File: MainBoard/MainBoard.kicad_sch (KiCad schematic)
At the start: 39 parts, among them J1 1761681-3, Q1 BC557, Q10 BC557, Q11 BC557, Q12 BC547, Q13 BC557, Q14 BC557, Q15 BC557, Q2 BC557, Q3 BC557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

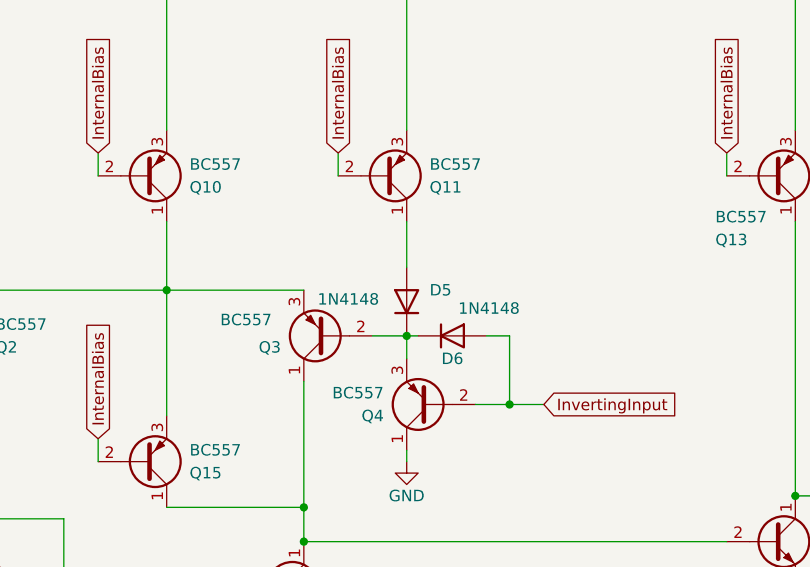
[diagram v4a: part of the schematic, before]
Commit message: added and assigned footprints
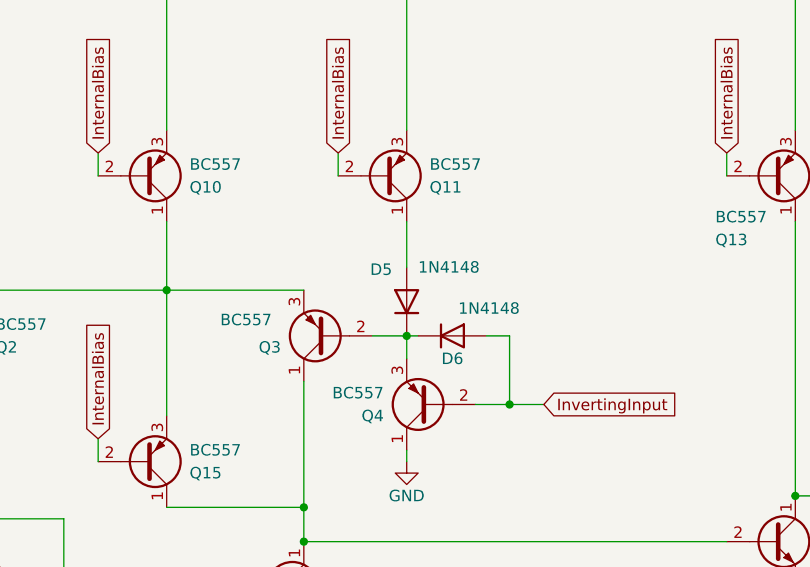
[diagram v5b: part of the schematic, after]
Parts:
- C1, C2: footprint (none) -> Capacitor_THT:CP_Radial_D10.0mm_P2.50mm
- C3, C4, C5, C6: footprint (none) -> Capacitor_THT:C_Disc_D5.0mm_W2.5mm_P2.50mm
- F1, F2: footprint (none) -> 72R020XU:FUSRB510W81L1358T310H1980
- R1, R2, R3, R4, R5, R6: footprint (none) -> Resistor_THT:R_Axial_DIN0309_L9.0mm_D3.2mm_P2.54mm_Vertical
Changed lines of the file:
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@@
 			)
 		)
-		(property "Footprint" ""
+		(property "Footprint" "Capacitor_THT:C_Disc_D5.0mm_W2.5mm_P2.50mm"
 			(at 153.9748 142.24 0)
 			(effects
@@
 			)
 		)
-		(property "Footprint" ""
+		(property "Footprint" "Capacitor_THT:CP_Radial_D10.0mm_P2.50mm"
 			(at 143.8148 152.4 0)
 			(effects
@@
 			)
 		)
-		(property "Footprint" ""
+		(property "Footprint" "72R020XU:FUSRB510W81L1358T310H1980"
 			(at 116.84 152.4 0)
 			(effects
@@
 			)
 		)
-		(property "Footprint" ""
+		(property "Footprint" "Capacitor_THT:CP_Radial_D10.0mm_P2.50mm"
 			(at 143.8148 142.24 0)
 			(effects
@@
 			)
 		)
-		(property "Footprint" ""
+		(property "Footprint" "Capacitor_THT:C_Disc_D5.0mm_W2.5mm_P2.50mm"
 			(at 165.4048 152.4 0)
 			(effects
@@
 			)
 		)
-		(property "Footprint" ""
+		(property "Footprint" "Capacitor_THT:C_Disc_D5.0mm_W2.5mm_P2.50mm"
 			(at 153.9748 152.4 0)
 			(effects
@@
 			)
 		)
-		(property "Footprint" ""
+		(property "Footprint" "Resistor_THT:R_Axial_DIN0309_L9.0mm_D3.2mm_P2.54mm_Vertical"
 			(at 52.832 38.1 90)
 			(effects
@@
 			)
 		)
-		(property "Footprint" ""
+		(property "Footprint" "Capacitor_THT:C_Disc_D5.0mm_W2.5mm_P2.50mm"
 			(at 165.4048 142.24 0)
 			(effects
@@
 			)
 		)
-		(property "Footprint" ""
+		(property "Footprint" "Resistor_THT:R_Axial_DIN0309_L9.0mm_D3.2mm_P2.54mm_Vertical"
 			(at 273.558 53.34 90)
 			(effects
@@
 			)
 		)
-		(property "Footprint" ""
+		(property "Footprint" "72R020XU:FUSRB510W81L1358T310H1980"
 			(at 116.84 132.08 0)
 			(effects
@@
 			)
 		)
-		(property "Footprint" ""
+		(property "Footprint" "Resistor_THT:R_Axial_DIN0309_L9.0mm_D3.2mm_P2.54mm_Vertical"
 			(at 230.378 43.18 90)
 			(effects
@@
 			)
 		)
-		(property "Footprint" ""
+		(property "Footprint" "Resistor_THT:R_Axial_DIN0309_L9.0mm_D3.2mm_P2.54mm_Vertical"
 			(at 52.832 27.94 90)
 			(effects
@@
 		(dnp no)
 		(property "Reference" "D5"
-			(at 160.02 55.8799 90)
+			(at 153.416 53.594 90)
 			(effects
 				(font
@@
 		)
 		(property "Value" "1N4148"
-			(at 147.574 56.896 90)
+			(at 158.75 53.34 90)
 			(effects
 				(font
@@
 			)
 		)
-		(property "Footprint" ""
+		(property "Footprint" "Resistor_THT:R_Axial_DIN0309_L9.0mm_D3.2mm_P2.54mm_Vertical"
 			(at 146.05 109.982 90)
 			(effects
@@
 			)
 		)
-		(property "Footprint" ""
+		(property "Footprint" "Resistor_THT:R_Axial_DIN0309_L9.0mm_D3.2mm_P2.54mm_Vertical"
 			(at 273.558 63.5 90)
 			(effects

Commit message: added pots for more control, tied low side to negative rail
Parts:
- removed C5, C6: 0.1uf, Capacitor_THT:C_Disc_D5.0mm_W2.5mm_P2.50mm, symbol Device:C
- removed R1, R2, R5: 1k, Resistor_THT:R_Axial_DIN0309_L9.0mm_D3.2mm_P2.54mm_Vertical, symbol Device:R
- removed R6: 11k, Resistor_THT:R_Axial_DIN0309_L9.0mm_D3.2mm_P2.54mm_Vertical, symbol Device:R
- added J2: Non-Inverting Input, THONK_PJ398SM-12, symbol PJ398SM-12:PJ398SM-12
- added J3: Inverting Input, THONK_PJ398SM-12, symbol PJ398SM-12:PJ398SM-12
- added J4: Output, THONK_PJ398SM-12, symbol PJ398SM-12:PJ398SM-12
- added RV1: 10k, symbol Device:R_Potentiometer_Trim
- added RV2: 100k, symbol Device:R_Potentiometer_Trim
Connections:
- net +v: now also RV1.1, RV2.1
- net -v: now also Q1.1 (C), Q12.3 (E), Q4.1 (C), Q5.3 (E), Q6.3 (E), Q7.3 (E), Q8.3 (E), RV2.3
- net GND: now also J2.1, J2.2, J3.1, J3.2, J4.1, J4.2, RV1.3; no longer Q1.1 (C), Q12.3 (E), Q4.1 (C), Q5.3 (E), Q6.3 (E), Q7.3 (E), Q8.3 (E)
- net InternalBias: now also RV1.2
- net InvertingInput: now also J3.3, RV2.2
- net NonInvertingInput: now also J2.3
- net Output: now also J4.3
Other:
- note added: ".options method=gear gmin=1e-9 cshunt=1e-12 .options reltol=1e-2 abstol=1e-9 vntol=1e-6 .options itl1=300 itl4=300 .options maxstep=100p temp=60 .tran 100u 1000ms .control run plot V(NonInvertingInput) V(InvertingInput) V(Output) .endc"
- note removed: ".options method=gear .options gmin=1e-9 cshunt=1e-12 .options reltol=1e-2 abstol=1e-9 vntol=1e-6 .options itl1=300 itl4=300 .options maxstep=100p .options temp=60 .tran 100u 1000ms .control run plot V(NonInvertingInput) V(InvertingInput) V(Output) .endc"
- moved on the sheet: C1, C2, C3, C4, D1, D2, D3, D4, D5, D6, F1, F2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

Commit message: enhanced smilulation
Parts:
- added V4: VPULSE, symbol Simulation_SPICE:VPULSE
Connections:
- net GND: now also V4.2
- net InvertingInput: now also V4.1
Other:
- moved on the sheet: J3

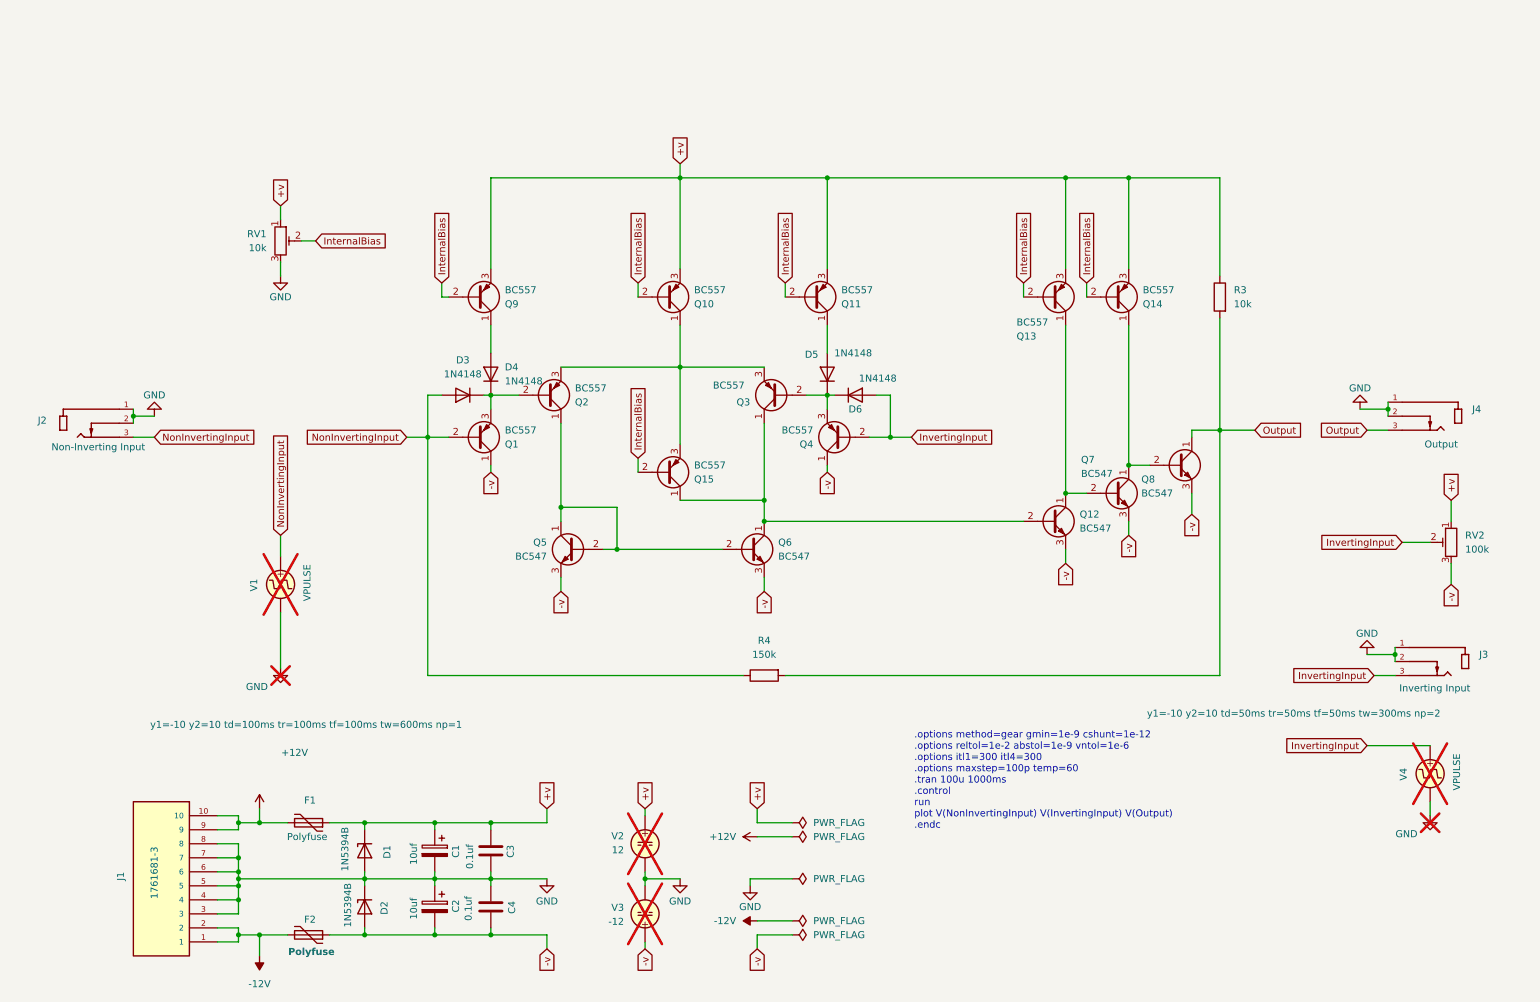
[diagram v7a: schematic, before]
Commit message: reduced hysterisis to prevent spikes on show rising edges, added over voltage protection on inputs and outputs
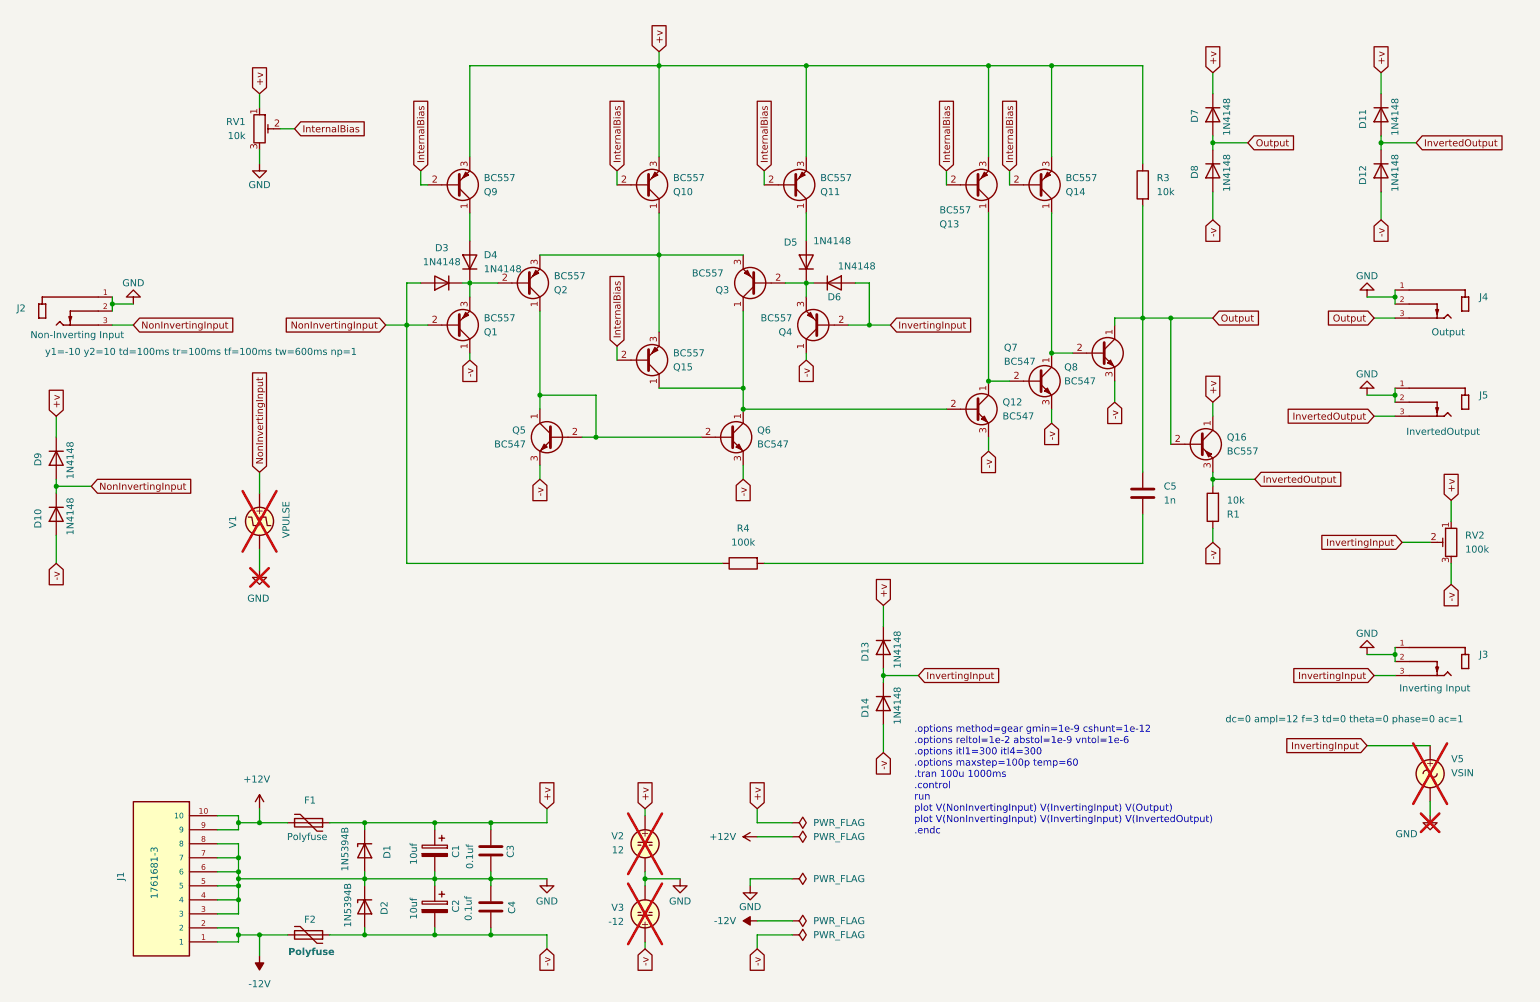
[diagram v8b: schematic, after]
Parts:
- removed V4: VPULSE, symbol Simulation_SPICE:VPULSE
- added C5: 1n, symbol Device:C
- added D10, D11, D12, D13, D14, D7, D8, D9: 1N4148, symbol Device:D
- added J5: InvertedOutput, THONK_PJ398SM-12, symbol PJ398SM-12:PJ398SM-12
- added Q16: BC557, Package_TO_SOT_THT:TO-92_Inline, symbol Transistor_BJT:BC557
- added R1: 10k, Resistor_THT:R_Axial_DIN0309_L9.0mm_D3.2mm_P2.54mm_Vertical, symbol Device:R
- added V5: VSIN, symbol Simulation_SPICE:VSIN
- R4: value 150k -> 100k
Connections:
- net +v: now also D11.1 (K), D13.1 (K), D7.1 (K), D9.1 (K), Q16.1 (C)
- net -v: now also D10.2 (A), D12.2 (A), D14.2 (A), D8.2 (A), R1.1
- net GND: now also J5.1, J5.2, V5.2
- net InvertingInput: now also D13.2 (A), D14.1 (K), V5.1
- net NonInvertingInput: now also D10.1 (K), D9.2 (A)
- net Output: now also C5.1, D7.2 (A), D8.1 (K), Q16.2 (B); no longer R4.2
- new net: C5.2, R4.2
- new net InvertedOutput: D11.2 (A), D12.1 (K), J5.3, Q16.3 (E), R1.2
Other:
- note added: ".options method=gear gmin=1e-9 cshunt=1e-12 .options reltol=1e-2 abstol=1e-9 vntol=1e-6 .options itl1=300 itl4=300 .options maxstep=100p temp=60 .tran 100u 1000ms .control run plot V(NonInvertingInput) V(InvertingInput) V(Output) plot V(NonInvertingInput) V(InvertingInput) V(InvertedOutput) .endc"
- note removed: ".options method=gear gmin=1e-9 cshunt=1e-12 .options reltol=1e-2 abstol=1e-9 vntol=1e-6 .options itl1=300 itl4=300 .options maxstep=100p temp=60 .tran 100u 1000ms .control run plot V(NonInvertingInput) V(InvertingInput) V(Output) .endc"
- moved on the sheet: D3, D4, D5, D6, J2, J4, Q1, Q10, Q11, Q12, Q13, Q14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
